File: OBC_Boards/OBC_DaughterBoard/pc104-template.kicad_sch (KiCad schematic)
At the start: 39 parts, among them J1 PC104_Connector, J10 Conn_01x04, J3 Conn_02x20_Odd_Even, J4 3.3V Input (Testing), J5 5V Input (Testing), J6 Conn_02x06_Odd_Even, J7 Conn_01x04, J8 Conn_01x04, J9 Conn_01x04, Q1 Q_PMOS_DGS, U2 MCP7940NT-I_MS, U3 BU33SA5WGWZ-E2-qsat-symb, U5 MCP3008

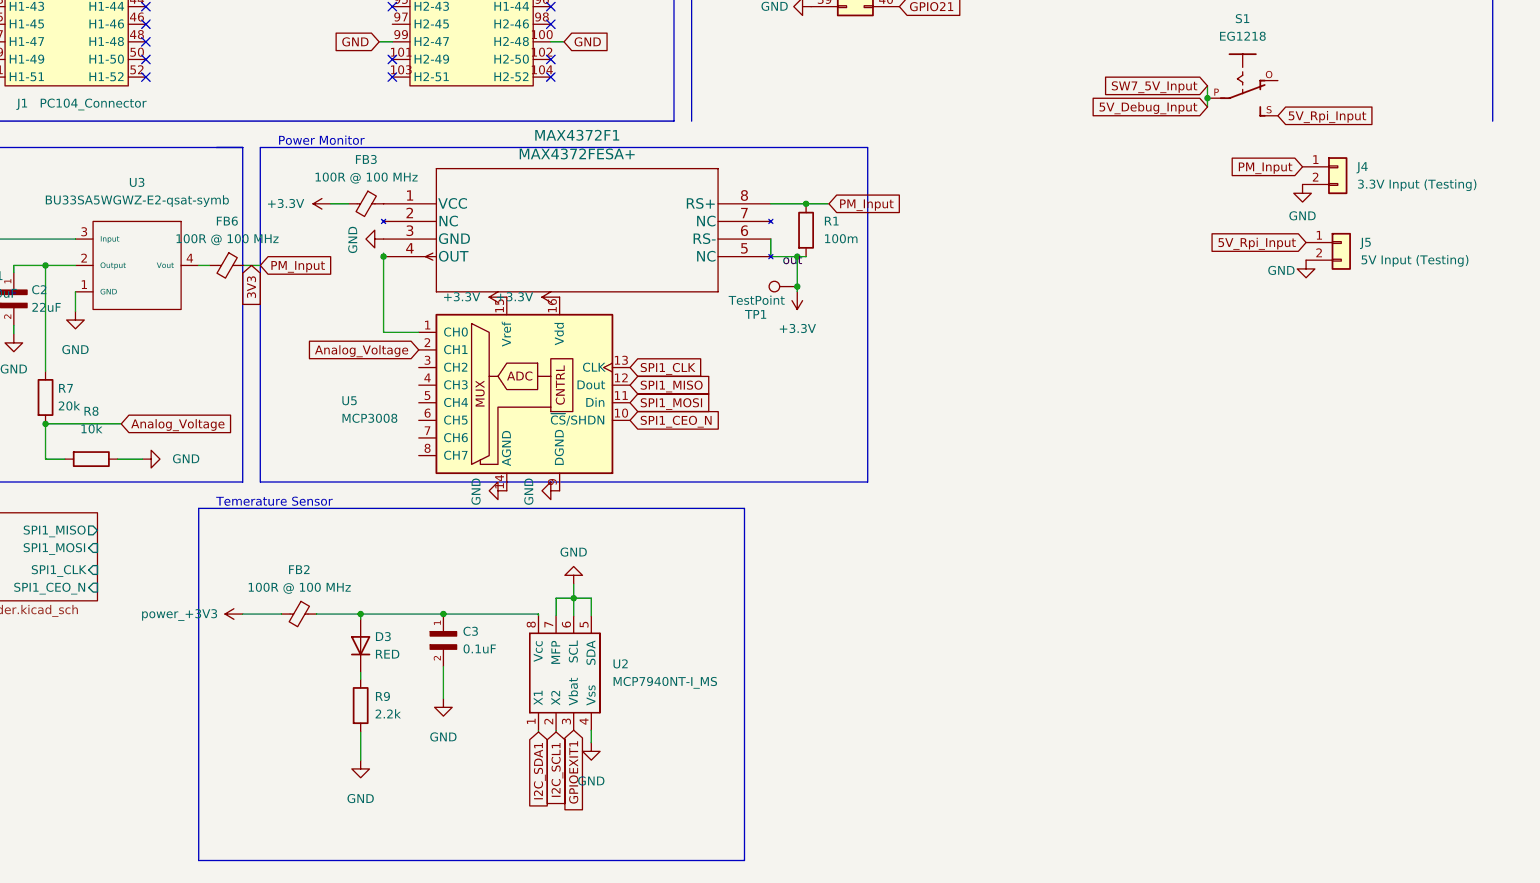
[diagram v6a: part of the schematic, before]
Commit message: obc: daughterboard: update power monitor to use hierarchical sheet
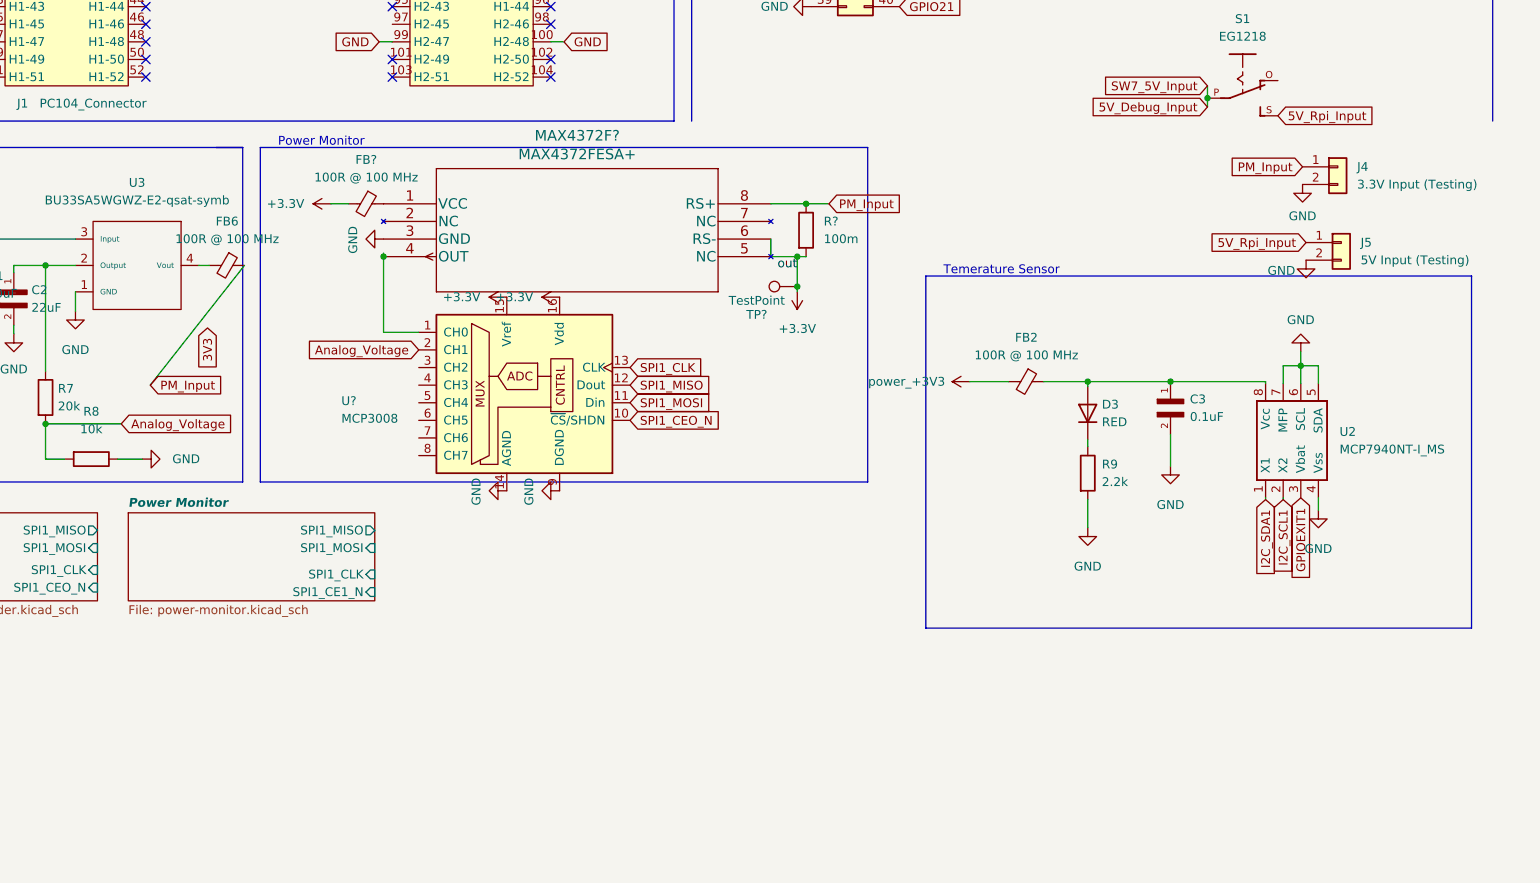
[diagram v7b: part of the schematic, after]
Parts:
- removed FB3: 100R @ 100 MHz, Daughterboard_footprints:BEADC1608X75N, symbol Device:FerriteBead_Small
- removed MAX4372F1: MAX4372FESA+, Max4372:Maxim-MAX4372FESA+-Level_A, symbol STM32_Breakout-rescue:MAX4372FESA+-MAX4372FESA+
- removed R1: 100m, Resistor_SMD:R_0201_0603Metric, symbol Device:R
- removed TP1: TestPoint, symbol Connector:TestPoint
- removed U5: MCP3008, MCP3008:Microchip-MCP3008-I_P-Manufacturer_Recommended, symbol Analog_ADC:MCP3008
- added FB?: 100R @ 100 MHz, Daughterboard_footprints:BEADC1608X75N, symbol Device:FerriteBead_Small
- added MAX4372F?: MAX4372FESA+, Max4372:Maxim-MAX4372FESA+-Level_A, symbol STM32_Breakout-rescue:MAX4372FESA+-MAX4372FESA+
- added R?: 100m, Resistor_SMD:R_0201_0603Metric, symbol Device:R
- added TP?: TestPoint, symbol Connector:TestPoint
- added U?: MCP3008, MCP3008:Microchip-MCP3008-I_P-Manufacturer_Recommended, symbol Analog_ADC:MCP3008
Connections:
- net +3V3: now also FB?.2, MAX4372F?.5 (NC), MAX4372F?.6 (RS-), R?.2, TP?.1, U?.15 (Vref), U?.16 (Vdd)
- net 3V3: no longer FB6.1, J4.1 (Pin_1)
- net Analog_Voltage: now also U?.2 (CH1)
- net GND: now also MAX4372F?.3 (GND), U?.14 (AGND), U?.9 (DGND)
- net SPI1_CEO_N: now also U?.10 (~{CS}/SHDN)
- net SPI1_CLK: now also U?.13 (CLK)
- net SPI1_MISO: now also U?.12 (Dout)
- net SPI1_MOSI: now also U?.11 (Din)
- new net: MAX4372F?.4 (OUT), U?.1 (CH0)
- new net: FB?.1, MAX4372F?.1 (VCC)
- new net PM_Input: FB6.1, J4.1 (Pin_1), MAX4372F?.8 (RS+), R?.1
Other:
- added sheet Power Monitor (power-monitor.kicad_sch)
- moved on the sheet: C3, D3, FB2, R9, U2

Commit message: temp sensor footprint
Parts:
- removed U2: MCP7940NT-I_MS, STM32_Breakout:MCP7940NT-I-MS, symbol Imported_OBC_Library:MCP7940NT-I_MS
- added U2: MCP9808T-E/MC, Daughterboard_footprints:SOP65P490X110-8N, symbol Daughterboard_Symbols:MCP9808T-E{brace}slash}MC
- TP1: renamed from TP?; footprint (none) -> TestPoint:TestPoint_2Pads_Pitch2.54mm_Drill0.8mm
- gave numbers to parts that had none: 4
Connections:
- net +3V3: no longer MAX4372F1.5 (NC)
- net GND: now also U2.4 (GND), U2.5 (A2), U2.6 (A1), U2.7 (A0), U2.9 (EPAD)
- net I2C_SCL1: now also U2.2 (SCL)
- net I2C_SDA1: now also U2.1 (SDA)
- net GPIO5: now reaches J3.29 (Pin_29)
- net GPIO5: now also U2.3 (ALERT)
- net at C3.1: now also D3.1 (A), FB2.1, U2.8 (VDD)
- no-connect marks 81 -> 83
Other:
- moved on the sheet: C3, D3, FB2, R9
